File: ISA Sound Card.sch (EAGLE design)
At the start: 89 parts, among them IC1 74LS07D, IC10 4051D, IC11 4051D, IC2 74AHC1G07DBV, IC3 74AC14D, IC4 74LVC1G125DBV, IC6 MCP3004, IC8 4051D, IC9 4051D, U1 PCM1808, U10 SN74LVC16T245DGGR, U11 SN74LVC16T245DGGR, U12 SN74LVC16T245DGGR, U3 MIC5365-3.3YD5-TR, U4 PCM5102, U7 MIC5365-3.3YD5-TR, U8 SN74LVC16T245DGGR, X2 LINE_OUT, X3 LINE_IN, X4_ D-SUB-15-SH

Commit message: Add Quartus project
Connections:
- net FPGA_0WS renamed FPGA_ZERO_WAIT
- net FPGA_SA159_DIR renamed FPGA_SA158_DIR
- net FPGA_SD159_DIR renamed FPGA_SD158_DIR
- removed net N$77: C60.1, U4.CPGND
- net ADC_3V3_FILT: no longer U1.MD1
- net GND: now also C60.1, U1.MD1, U4.CPGND, U4.SCK; no longer CYC_IV_G$1.CLK14_6N@6, CYC_IV_G$1.CLK15_6P@5
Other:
- note added: "CLK inputs Grounded on the proto! ->"
- note added: "Pins 11 (MD1) was not grounded! MD1 and MD0 need to both be Low for SLAVE mode."
- note added: "Pins 3 and 12 were not grounded !"
- note added: "SCK pin should really be Grounded. The DAC will internally generate it using BCK."
- note added: "Should probably add a resistor between the X pin and 5V on these..."
- moved on the sheet: R4
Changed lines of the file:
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@@
 <text x="195.58" y="-50.8" size="1.778" layer="97">&lt;- Open-Drain Outputs</text>
 <text x="76.2" y="129.54" size="1.778" layer="97">&lt;- BIDIR -&gt;</text>
+<text x="307.34" y="30.48" size="2.54" layer="91">Should probably add a resistor between the X pin and 5V on these...</text>
 </plain>
 <instances>
@@
 <attribute name="VALUE" x="69.85" y="110.998" size="1.778" layer="96"/>
 </instance>
-<instance part="+3V11" gate="G$1" x="284.48" y="-121.92" rot="R270"/>
-<instance part="R4" gate="G$1" x="271.78" y="-121.92" rot="MR0">
-<attribute name="NAME" x="275.59" y="-120.4214" size="1.778" layer="95" rot="MR0"/>
-<attribute name="VALUE" x="275.59" y="-125.222" size="1.778" layer="96" rot="MR0"/>
+<instance part="+3V11" gate="G$1" x="292.1" y="-121.92" rot="R270"/>
+<instance part="R4" gate="G$1" x="279.4" y="-121.92" rot="MR0">
+<attribute name="NAME" x="283.21" y="-120.4214" size="1.778" layer="95" rot="MR0"/>
+<attribute name="VALUE" x="283.21" y="-125.222" size="1.778" layer="96" rot="MR0"/>
 </instance>
 <instance part="+3V2" gate="G$1" x="297.18" y="-60.96" rot="R270"/>
@@
 </segment>
 </net>
-<net name="FPGA_0WS" class="0">
+<net name="FPGA_ZERO_WAIT" class="0">
 <segment>
 <pinref part="IC2" gate="A" pin="I"/>
 <label x="248.92" y="-121.92" size="1.778" layer="95"/>
 <pinref part="R4" gate="G$1" pin="2"/>
-<wire x1="246.38" y1="-121.92" x2="266.7" y2="-121.92" width="0.1524" layer="91"/>
+<wire x1="246.38" y1="-121.92" x2="274.32" y2="-121.92" width="0.1524" layer="91"/>
 </segment>
 </net>
@@
 <pinref part="R4" gate="G$1" pin="1"/>
 <pinref part="+3V11" gate="G$1" pin="+3V3"/>
-<wire x1="276.86" y1="-121.92" x2="281.94" y2="-121.92" width="0.1524" layer="91"/>
+<wire x1="284.48" y1="-121.92" x2="289.56" y2="-121.92" width="0.1524" layer="91"/>
 </segment>
 <segment>
@@
 </segment>
 </net>
-<net name="FPGA_SD159_DIR" class="0">
+<net name="FPGA_SD158_DIR" class="0">
 <segment>
 <pinref part="U12" gate="G$1" pin="2DIR"/>
@@
 </segment>
 </net>
-<net name="FPGA_SA159_DIR" class="0">
+<net name="FPGA_SA158_DIR" class="0">
 <segment>
 <pinref part="U8" gate="G$1" pin="1DIR"/>
@@
 <description>FPGA</description>
 <plain>
+<text x="-5.08" y="99.06" size="1.778" layer="97">CLK inputs Grounded on the proto! -&gt;</text>
 </plain>
 <instances>
@@
 </segment>
 </net>
-<net name="FPGA_0WS" class="0">
+<net name="FPGA_ZERO_WAIT" class="0">
 <segment>
 <wire x1="104.14" y1="50.8" x2="96.52" y2="50.8" width="0.1524" layer="91"/>
@@
 <segment>
 <pinref part="GND7" gate="1" pin="GND"/>
-<wire x1="40.64" y1="104.14" x2="38.1" y2="104.14" width="0.1524" layer="91"/>
-<wire x1="38.1" y1="104.14" x2="33.02" y2="104.14" width="0.1524" layer="91"/>
-<wire x1="40.64" y1="99.06" x2="38.1" y2="99.06" width="0.1524" layer="91"/>
-<wire x1="38.1" y1="99.06" x2="38.1" y2="104.14" width="0.1524" layer="91"/>
-<junction x="38.1" y="104.14"/>
+<wire x1="40.64" y1="104.14" x2="33.02" y2="104.14" width="0.1524" layer="91"/>
 <pinref part="CYC_IV_" gate="G$1" pin="GND@1"/>
-<pinref part="CYC_IV_" gate="G$1" pin="CLK15_6P@5"/>
 </segment>
 <segment>
 <pinref part="GND8" gate="1" pin="GND"/>
-<wire x1="96.52" y1="104.14" x2="99.06" y2="104.14" width="0.1524" layer="91"/>
-<wire x1="99.06" y1="104.14" x2="104.14" y2="104.14" width="0.1524" layer="91"/>
-<wire x1="96.52" y1="99.06" x2="99.06" y2="99.06" width="0.1524" layer="91"/>
-<wire x1="99.06" y1="99.06" x2="99.06" y2="104.14" width="0.1524" layer="91"/>
-<junction x="99.06" y="104.14"/>
+<wire x1="96.52" y1="104.14" x2="104.14" y2="104.14" width="0.1524" layer="91"/>
 <pinref part="CYC_IV_" gate="G$1" pin="GND@2"/>
-<pinref part="CYC_IV_" gate="G$1" pin="CLK14_6N@6"/>
 </segment>
 <segment>
@@
 </segment>
 </net>
-<net name="FPGA_SD159_DIR" class="0">
+<net name="FPGA_SD158_DIR" class="0">
 <segment>
 <wire x1="104.14" y1="73.66" x2="96.52" y2="73.66" width="0.1524" layer="91"/>
@@
 </segment>
 </net>
-<net name="FPGA_SA159_DIR" class="0">
+<net name="FPGA_SA158_DIR" class="0">
 <segment>
 <wire x1="170.18" y1="48.26" x2="162.56" y2="48.26" width="0.1524" layer="91"/>
@@
 <plain>
 <text x="147.32" y="114.3" size="1.778" layer="91">&lt;- Standard I2S</text>
+<text x="93.98" y="147.32" size="1.778" layer="91">Pins 3 and 12 were not grounded !</text>
+<text x="154.94" y="99.06" size="1.778" layer="91">SCK pin should really be Grounded.
+The DAC will internally generate it using BCK.</text>
+<text x="121.92" y="55.88" size="1.778" layer="91">Pins 11 (MD1) was not grounded!
+MD1 and MD0 need to both be Low for SLAVE mode.</text>
 </plain>
 <instances>
@@
 <pinref part="GND50" gate="1" pin="GND"/>
 <wire x1="142.24" y1="114.3" x2="144.78" y2="114.3" width="0.1524" layer="91"/>
-<wire x1="144.78" y1="114.3" x2="144.78" y2="101.6" width="0.1524" layer="91"/>
+<wire x1="144.78" y1="114.3" x2="144.78" y2="104.14" width="0.1524" layer="91"/>
+<wire x1="144.78" y1="104.14" x2="144.78" y2="101.6" width="0.1524" layer="91"/>
 <wire x1="144.78" y1="101.6" x2="144.78" y2="99.06" width="0.1524" layer="91"/>
 <wire x1="142.24" y1="121.92" x2="144.78" y2="121.92" width="0.1524" layer="91"/>
@@
 <pinref part="U4" gate="G$1" pin="FMT"/>
 <pinref part="U4" gate="G$1" pin="FLT"/>
+<pinref part="U4" gate="G$1" pin="SCK"/>
+<wire x1="142.24" y1="104.14" x2="144.78" y2="104.14" width="0.1524" layer="91"/>
+<junction x="144.78" y="104.14"/>
 </segment>
 <segment>
@@
 <pinref part="GND18" gate="1" pin="GND"/>
 <wire x1="142.24" y1="30.48" x2="144.78" y2="30.48" width="0.1524" layer="91"/>
-<wire x1="144.78" y1="30.48" x2="144.78" y2="25.4" width="0.1524" layer="91"/>
+<wire x1="144.78" y1="30.48" x2="144.78" y2="27.94" width="0.1524" layer="91"/>
 <pinref part="U1" gate="G$1" pin="MD0"/>
+<wire x1="144.78" y1="27.94" x2="144.78" y2="25.4" width="0.1524" layer="91"/>
 <wire x1="144.78" y1="25.4" x2="144.78" y2="17.78" width="0.1524" layer="91"/>
 <wire x1="142.24" y1="25.4" x2="144.78" y2="25.4" width="0.1524" layer="91"/>
 <junction x="144.78" y="25.4"/>
+<pinref part="U1" gate="G$1" pin="MD1"/>
+<wire x1="142.24" y1="27.94" x2="144.78" y2="27.94" width="0.1524" layer="91"/>
+<junction x="144.78" y="27.94"/>
 </segment>
 <segment>
@@
 <wire x1="101.6" y1="93.98" x2="111.76" y2="93.98" width="0.1524" layer="91"/>
 <junction x="111.76" y="93.98"/>
+<pinref part="C60" gate="G$1" pin="1"/>
+<wire x1="104.14" y1="134.62" x2="106.68" y2="134.62" width="0.1524" layer="91"/>
+<wire x1="106.68" y1="134.62" x2="106.68" y2="119.38" width="0.1524" layer="91"/>
+<wire x1="106.68" y1="119.38" x2="109.22" y2="119.38" width="0.1524" layer="91"/>
+<pinref part="U4" gate="G$1" pin="CPGND"/>
+<wire x1="109.22" y1="119.38" x2="114.3" y2="119.38" width="0.1524" layer="91"/>
+<wire x1="109.22" y1="119.38" x2="109.22" y2="104.14" width="0.1524" layer="91"/>
+<wire x1="109.22" y1="104.14" x2="111.76" y2="104.14" width="0.1524" layer="91"/>
+<junction x="109.22" y="119.38"/>
+<junction x="111.76" y="104.14"/>
 </segment>
 <segment>
@@
 </segment>
 </net>
-<net name="N$77" class="0">
-<segment>
-<pinref part="C60" gate="G$1" pin="1"/>
-<wire x1="104.14" y1="134.62" x2="106.68" y2="134.62" width="0.1524" layer="91"/>
-<wire x1="106.68" y1="134.62" x2="106.68" y2="119.38" width="0.1524" layer="91"/>
-<wire x1="106.68" y1="119.38" x2="114.3" y2="119.38" width="0.1524" layer="91"/>
-<pinref part="U4" gate="G$1" pin="CPGND"/>
-</segment>
-</net>
 <net name="N$62" class="0">
 <segment>
@@
 <junction x="83.82" y="27.94"/>
 </segment>
-<segment>
-<pinref part="U1" gate="G$1" pin="MD1"/>
-<wire x1="142.24" y1="27.94" x2="152.4" y2="27.94" width="0.1524" layer="91"/>
-<label x="149.86" y="27.94" size="1.778" layer="95"/>
-</segment>
 </net>

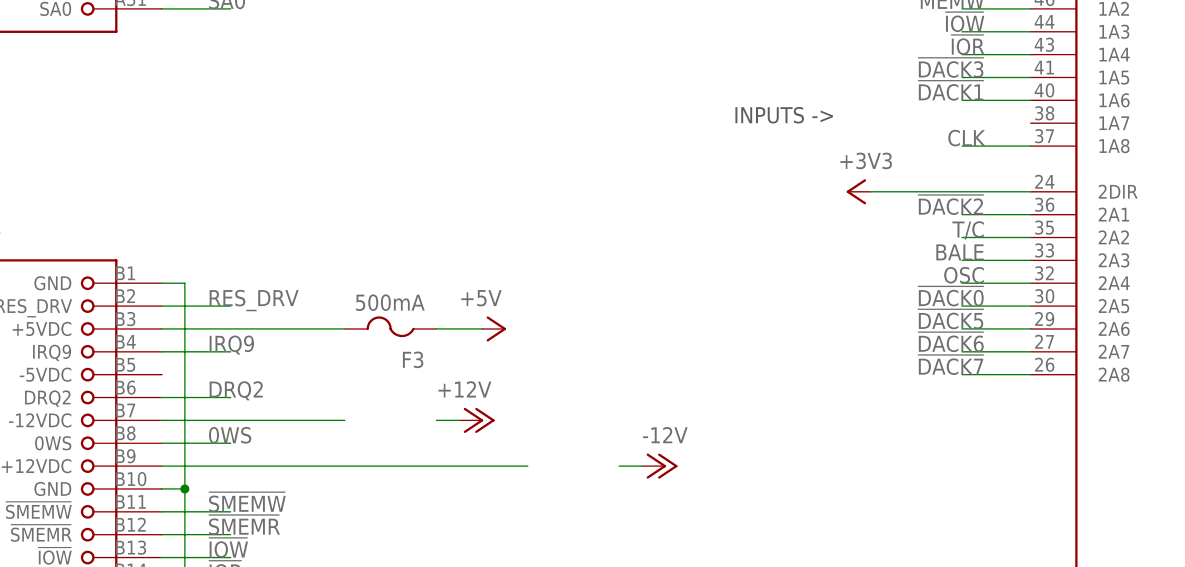
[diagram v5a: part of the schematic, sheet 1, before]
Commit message: Hooked up ISA CLK and OSC to the FPGA Clk-in pins
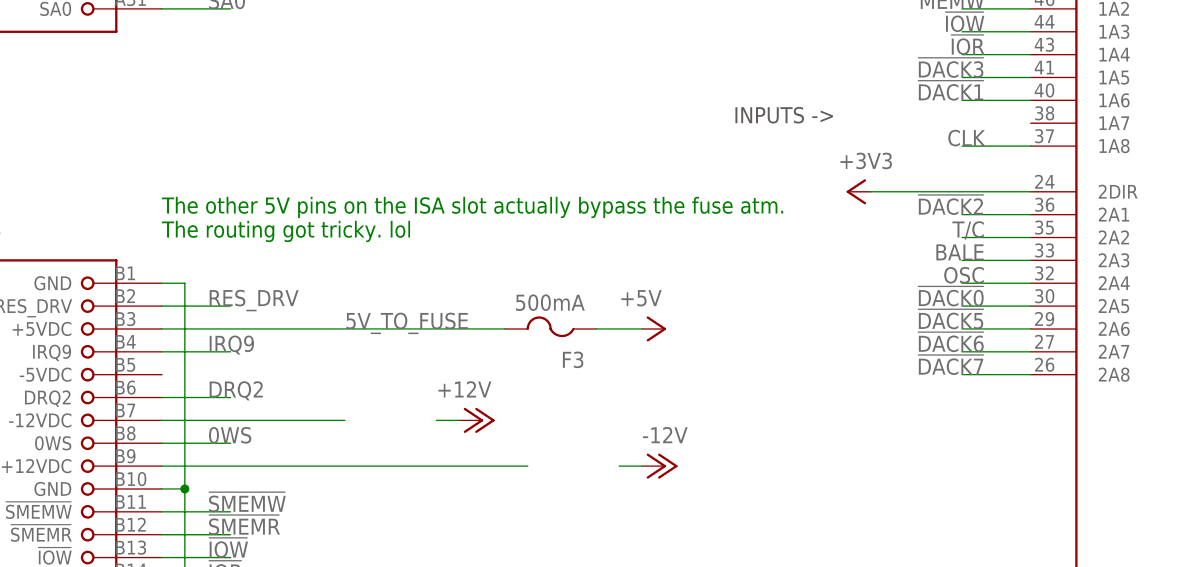
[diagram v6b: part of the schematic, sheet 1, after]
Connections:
- net N$13 renamed 5V_TO_FUSE
- net FPGA_CLK: now also CYC_IV_G$1.CLK15_6P@5; no longer CYC_IV_G$2.B1@25
- net FPGA_OSC: now also CYC_IV_G$1.CLK14_6N@6; no longer CYC_IV_G$2.C1@23
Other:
- note added: "CLK inputs were Grounded on the proto! ->"
- note added: "The other 5V pins on the ISA slot actually bypass the fuse atm. The routing got tricky. lol"
- note removed: "CLK inputs Grounded on the proto! ->"
- moved on the sheet: F3
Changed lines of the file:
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@@
 <text x="76.2" y="129.54" size="1.778" layer="97">&lt;- BIDIR -&gt;</text>
 <text x="307.34" y="30.48" size="2.54" layer="91">Should probably add a resistor between the X pin and 5V on these...</text>
+<text x="12.7" y="2.54" size="1.778" layer="91">The other 5V pins on the ISA slot actually bypass the fuse atm.
+The routing got tricky. lol</text>
 </plain>
 <instances>
@@
 <instance part="GND4" gate="1" x="15.24" y="-157.48" rot="MR0"/>
 <instance part="GND5" gate="1" x="15.24" y="-83.82" rot="MR0"/>
-<instance part="P+1" gate="1" x="50.8" y="-7.62" rot="R270"/>
+<instance part="P+1" gate="1" x="68.58" y="-7.62" rot="R270"/>
 <instance part="P+3" gate="1" x="48.26" y="-17.78" rot="R270"/>
 <instance part="P-3" gate="1" x="68.58" y="-22.86" rot="MR270"/>
@@
 <instance part="GND27" gate="1" x="231.14" y="124.46" rot="MR0"/>
 <instance part="GND28" gate="1" x="231.14" y="88.9" rot="MR0"/>
-<instance part="F3" gate="G$1" x="38.1" y="-5.08" rot="R180"/>
+<instance part="F3" gate="G$1" x="55.88" y="-5.08" rot="R180"/>
 <instance part="IC8" gate="A" x="358.14" y="2.54"/>
 <instance part="IC9" gate="A" x="358.14" y="-43.18"/>
@@
 <pinref part="F3" gate="G$1" pin="1"/>
 <pinref part="P+1" gate="1" pin="+5V"/>
-<wire x1="43.18" y1="-7.62" x2="48.26" y2="-7.62" width="0.1524" layer="91"/>
+<wire x1="60.96" y1="-7.62" x2="66.04" y2="-7.62" width="0.1524" layer="91"/>
 </segment>
 <segment>
@@
 </segment>
 </net>
-<net name="N$13" class="0">
+<net name="5V_TO_FUSE" class="0">
 <segment>
 <pinref part="ISA" gate="B" pin="+5VDC@1"/>
 <pinref part="F3" gate="G$1" pin="2"/>
-<wire x1="12.7" y1="-7.62" x2="33.02" y2="-7.62" width="0.1524" layer="91"/>
+<wire x1="12.7" y1="-7.62" x2="50.8" y2="-7.62" width="0.1524" layer="91"/>
+<label x="33.02" y="-7.62" size="1.778" layer="95"/>
 </segment>
 </net>
@@
 <description>FPGA</description>
 <plain>
-<text x="-5.08" y="99.06" size="1.778" layer="97">CLK inputs Grounded on the proto! -&gt;</text>
+<text x="-7.62" y="99.06" size="1.778" layer="97" rot="MR0">CLK inputs were Grounded on the proto! -&gt;</text>
 </plain>
 <instances>
@@
 <net name="FPGA_CLK" class="0">
 <segment>
-<wire x1="170.18" y1="71.12" x2="162.56" y2="71.12" width="0.1524" layer="91"/>
-<label x="165.1" y="71.12" size="1.778" layer="95" align="bottom-right"/>
-<pinref part="CYC_IV_" gate="G$2" pin="B1@25"/>
+<pinref part="CYC_IV_" gate="G$1" pin="CLK15_6P@5"/>
+<wire x1="40.64" y1="99.06" x2="33.02" y2="99.06" width="0.1524" layer="91"/>
+<label x="35.56" y="99.06" size="1.778" layer="95" rot="MR0"/>
 </segment>
 </net>
@@
 <net name="FPGA_OSC" class="0">
 <segment>
-<wire x1="170.18" y1="73.66" x2="162.56" y2="73.66" width="0.1524" layer="91"/>
-<label x="165.1" y="73.66" size="1.778" layer="95" align="bottom-right"/>
-<pinref part="CYC_IV_" gate="G$2" pin="C1@23"/>
+<pinref part="CYC_IV_" gate="G$1" pin="CLK14_6N@6"/>
+<wire x1="96.52" y1="99.06" x2="104.14" y2="99.06" width="0.1524" layer="91"/>
+<label x="101.6" y="99.06" size="1.778" layer="95"/>
 </segment>
 </net>

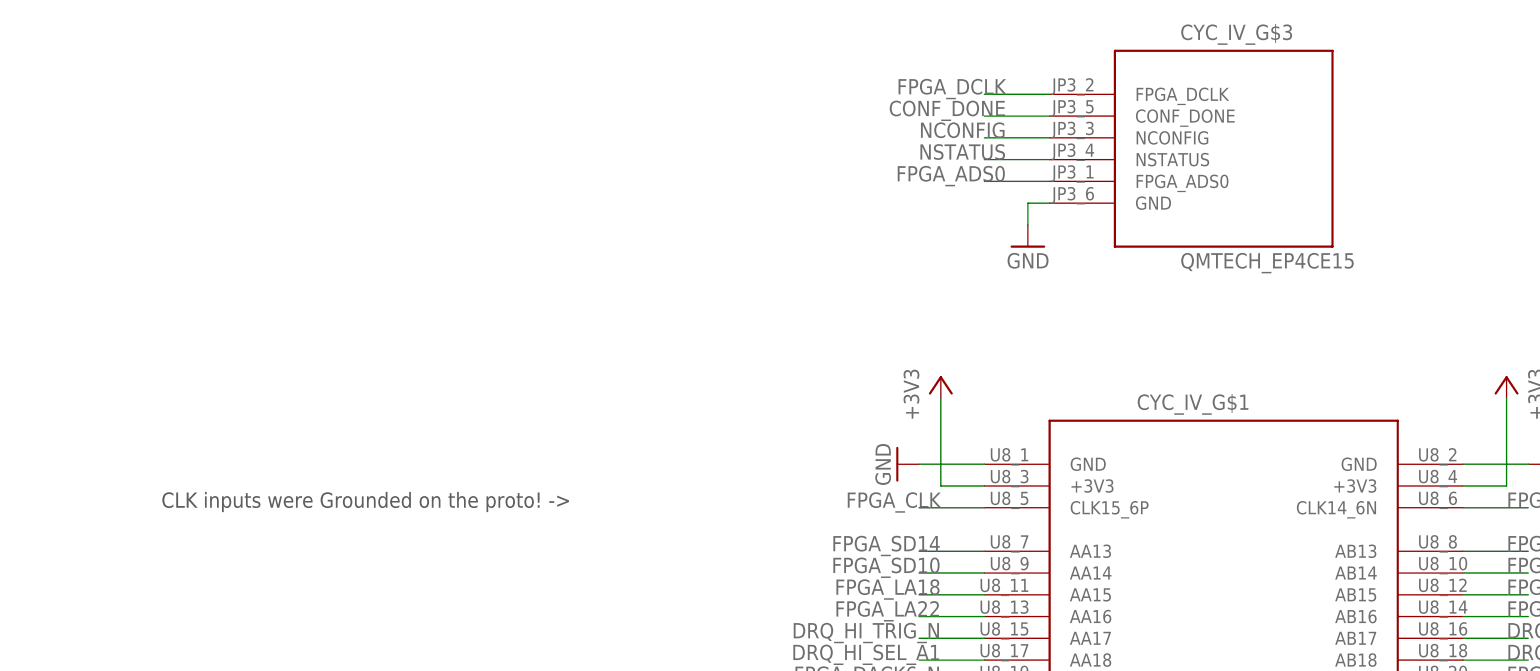
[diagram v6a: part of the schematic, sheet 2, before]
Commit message: Changed joystick port DB15 for the correct (female) connector
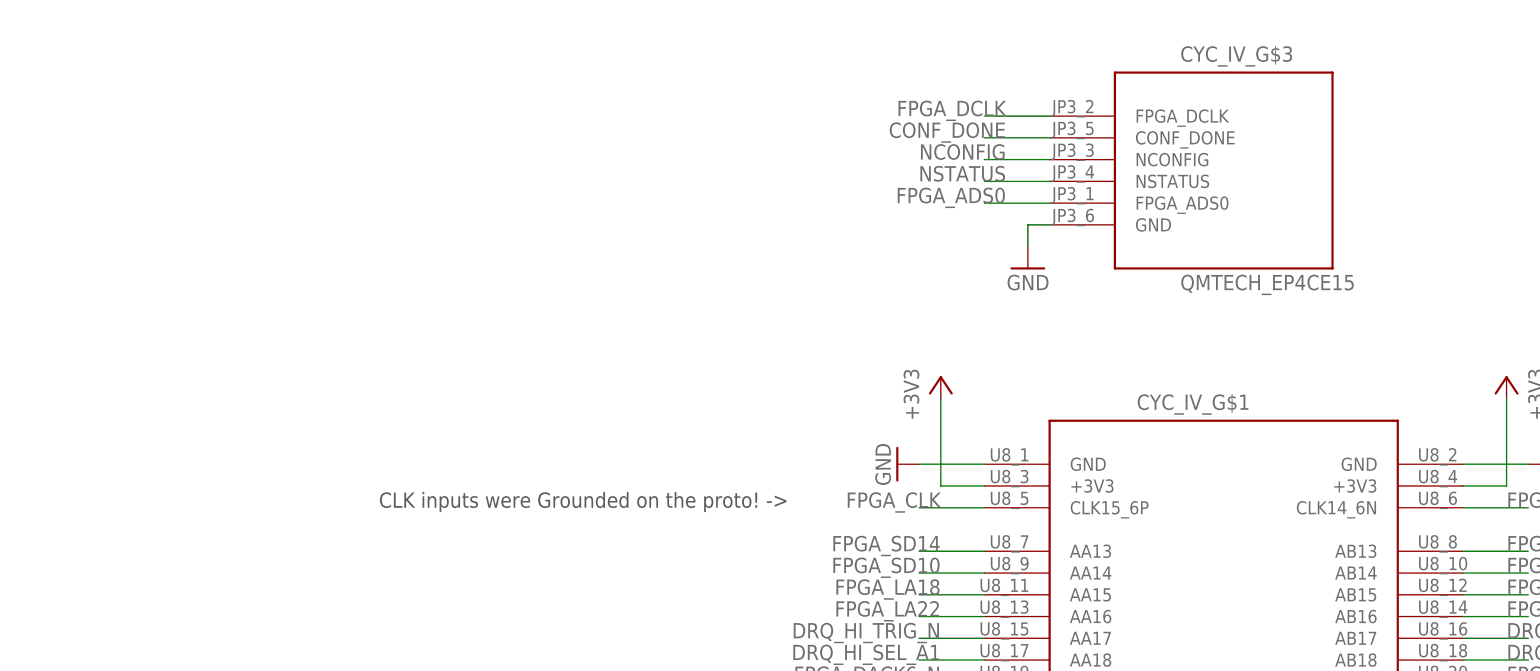
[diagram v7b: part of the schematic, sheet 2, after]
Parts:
- removed X4_: D-SUB-15-SH, con-thomas-betts:D-SUB-15-SH
- added X1: D-SUB15-H5R15RA, con-thomas-betts:D-SUB15-H5R15RA
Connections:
- net +5V: now also X1-1.F, X1-8.F, X1-9.F; no longer X4_1.F, X4_8.F, X4_9.F
- net GND: now also X1-4.F, X1-5.F; no longer X4_4.F, X4_5.F
- net JOY_B1_N: now also X1-2.F; no longer X4_2.F
- net JOY_B2_N: now also X1-7.F; no longer X4_7.F
- net JOY_B3_N: now also X1-10.F; no longer X4_10.F
- net JOY_B4_N: now also X1-14.F; no longer X4_14.F
- net JOY_X1: now also X1-3.F; no longer X4_3.F
- net JOY_X2: now also X1-11.F; no longer X4_11.F
- net JOY_Y1: now also X1-6.F; no longer X4_6.F
- net JOY_Y2: now also X1-13.F; no longer X4_13.F
- net MIDI_RXD: now also X1-12.F; no longer X4_12.F
- net MIDI_TXD: now also X1-15.F; no longer X4_15.F
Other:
- note added: "<- Not used."
- moved on the sheet: CYC_IV_G$3
